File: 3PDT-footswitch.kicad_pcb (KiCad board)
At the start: 2 copper layers, 27.7 x 25.1 mm, 14 parts

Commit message: improved simple routing
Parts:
- moved TP106 25.3 mm to (121.0, 83.8)
- moved TP105 25.0 mm to (121.0, 79.0)
- moved TP103 17.3 mm to (136.0, 92.3), turned to -90 degrees
- moved TP102 16.5 mm to (130.6, 92.3), turned to -90 degrees
- moved TP108 6.05 mm to (145.6, 79.0)
- moved TP109 4.85 mm to (145.6, 83.8)
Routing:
- net /A_RIGHT: track 21.2 -> 7.92 mm
- net /A_LEFT: track 20.6 -> 7.92 mm
- net /IN_RIGHT: track 15.2 -> 7.34 mm
- net /IN_LEFT: track 14.8 -> 12.1 mm
- net /B_LEFT: track 8.58 -> 7.97 mm
- net GND: vias 41 -> 39

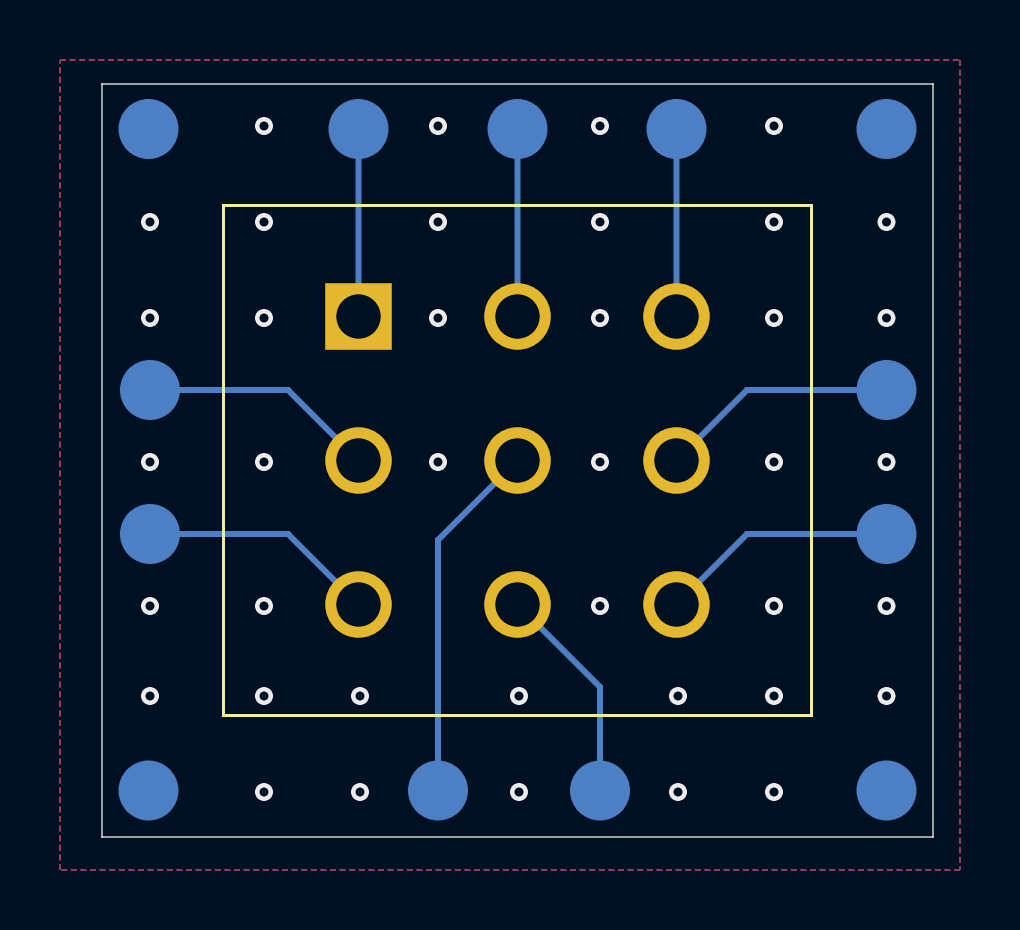
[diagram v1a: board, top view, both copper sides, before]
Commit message: smaller pcb, added silkscreens
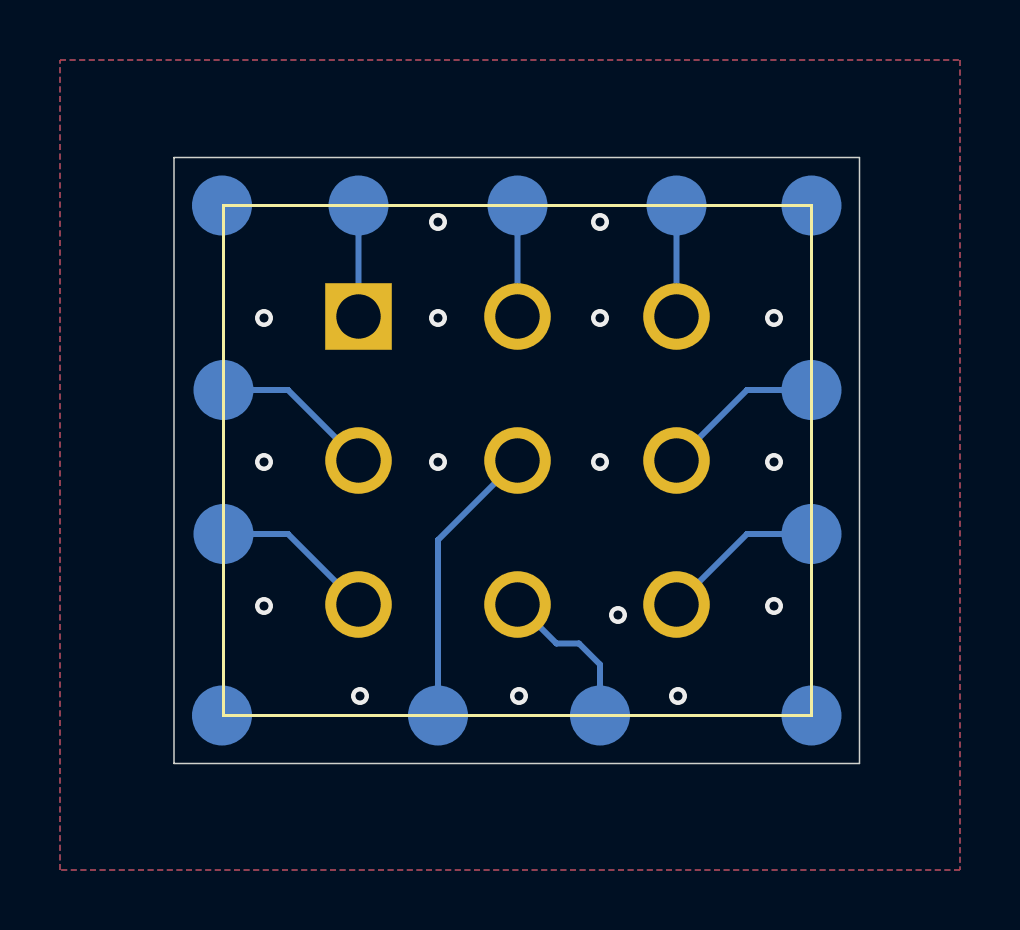
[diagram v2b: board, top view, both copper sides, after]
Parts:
- moved TP111 3.57 mm to (143.1, 72.8)
- moved TP110 3.54 mm to (123.4, 72.8)
- moved TP113 3.54 mm to (143.1, 89.8)
- moved TP112 3.50 mm to (123.4, 89.8)
- moved TP101 2.55 mm to (133.2, 72.8)
- moved TP104 2.55 mm to (128.0, 72.8)
- moved TP107 2.55 mm to (138.6, 72.8)
- moved TP102 2.50 mm to (130.6, 89.8)
- moved TP103 2.50 mm to (136.0, 89.8)
- moved TP108 2.50 mm to (143.1, 79.0)
- moved TP109 2.50 mm to (143.1, 83.8)
- moved TP105 2.45 mm to (123.5, 79.0)
- moved TP106 2.45 mm to (123.5, 83.8)
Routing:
- net /V+: track 6.25 -> 3.70 mm
- net /DETECT_B: track 6.25 -> 3.70 mm
- net /DETECT_A: track 6.25 -> 3.70 mm
- net /IN_LEFT: track 12.1 -> 9.60 mm
- net /B_RIGHT: track 7.97 -> 5.47 mm
- net /B_LEFT: track 7.97 -> 5.47 mm
- net /A_RIGHT: track 7.92 -> 5.47 mm
- net /A_LEFT: track 7.92 -> 5.47 mm
- net /IN_RIGHT: track 7.34 -> 5.28 mm
- net GND: vias 39 -> 16
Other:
- board size 27.7 x 25.1 mm -> 22.9 x 20.2 mm
- board text added: "1"
- board text added: "A1"
- board text added: "A2"
- board text added: "B1"
- board text added: "B2"
- board text added: "DETA"
- board text added: "DETB"
- board text added: "GND"
- board text added: "IN1"
- board text added: "IN2"
- board text added: "VDET"

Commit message: added footswitch id to silkscreen
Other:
- board text added: "3PDT (SF17010F-0302)"
